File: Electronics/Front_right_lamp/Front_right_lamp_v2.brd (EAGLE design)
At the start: 42.9 x 26.7 mm, 9 parts

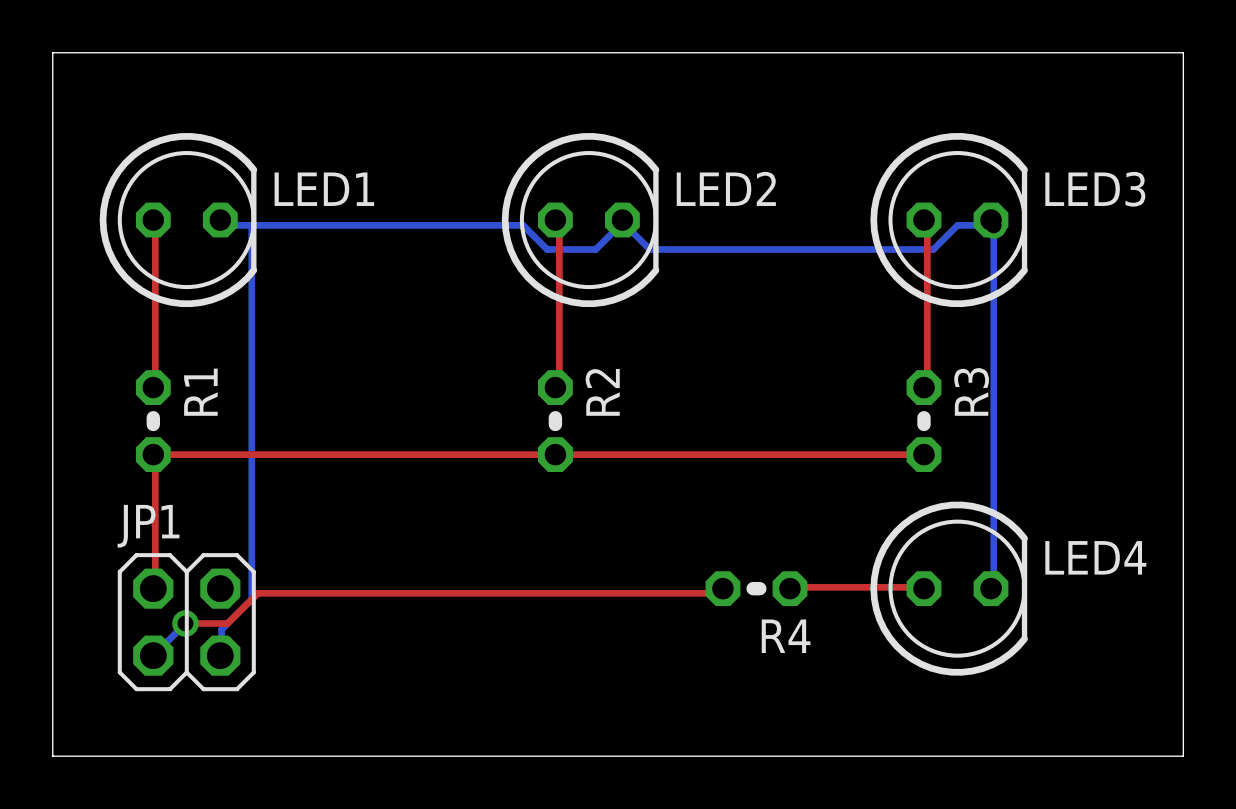
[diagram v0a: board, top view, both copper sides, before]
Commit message: Front lamps done
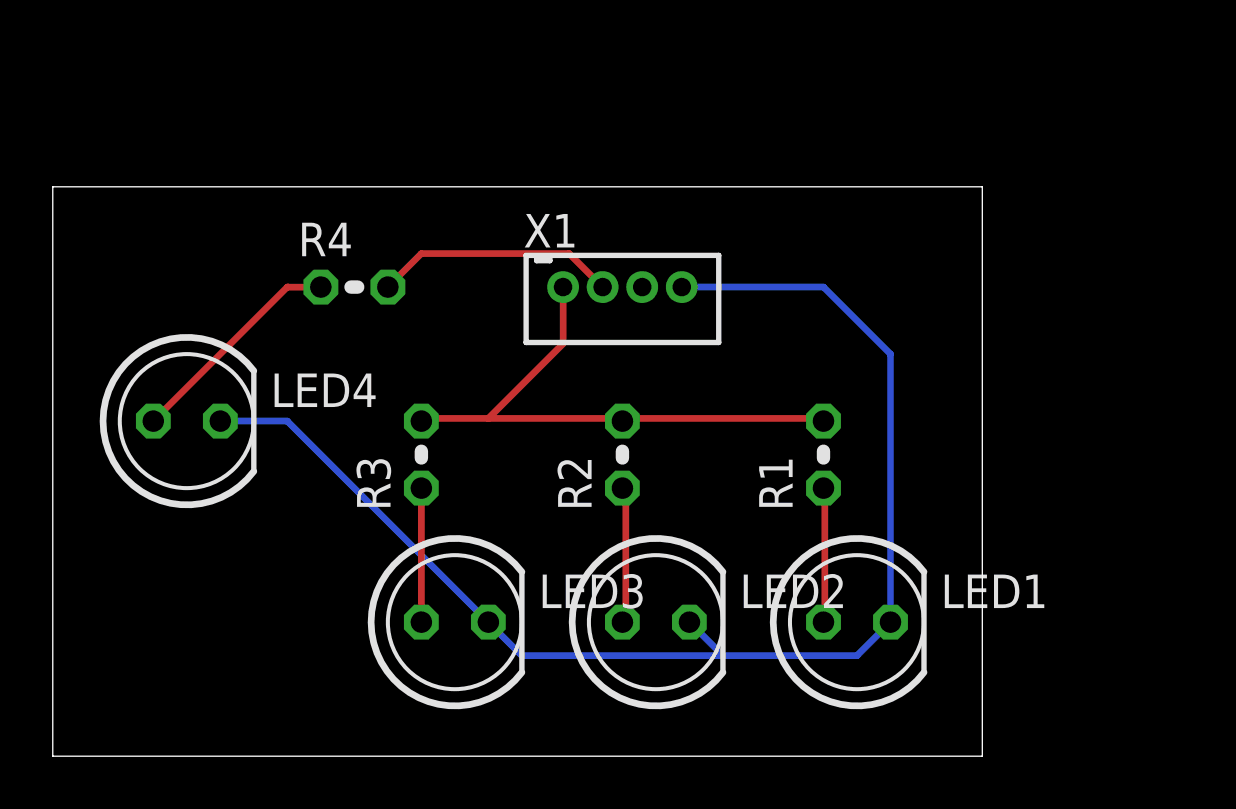
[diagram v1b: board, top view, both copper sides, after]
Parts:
- removed JP1: 2X2, pinhead:2X02
- added X1: B4B-ZR, con-jst:B4B-ZR
- LED1, LED2, LED3: value 2.58V -> 2.58 V
- LED4: value 2.88V -> 1.88 V
- R4: value 1K -> 680
- moved LED4 29.9 mm to (5.08, 12.7)
- moved LED1 29.6 mm to (30.5, 5.08)
- moved R1 25.4 mm to (29.2, 11.4), turned to 90 degrees
- moved LED3 24.4 mm to (15.2, 5.08)
- moved R3 19.1 mm to (14.0, 11.4), turned to 90 degrees
- moved R4 19.1 mm to (11.4, 17.8), turned to 0 degrees
- moved LED2 15.5 mm to (22.9, 5.08)
- moved R2 2.84 mm to (21.6, 11.4), turned to 90 degrees
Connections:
- net N$5: now also X1.1; no longer JP1.2
- net N$6: now also X1.2; no longer JP1.1
- net N$7: now also X1.4; no longer JP1.3
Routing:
- net N$6: track 22.7 -> 9.19 mm, vias 1 -> 0
- net N$5: track 34.3 -> 21.5 mm
- net N$7: track 62.1 -> 50.5 mm, vias 2 -> 0
- net N$4: track 5.10 -> 8.45 mm
- net N$3: track 6.42 -> 5.08 mm
- net N$1: track 6.38 -> 5.10 mm
- net N$2: track 6.45 -> 5.18 mm
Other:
- board size 42.9 x 26.7 mm -> 35.2 x 21.6 mm

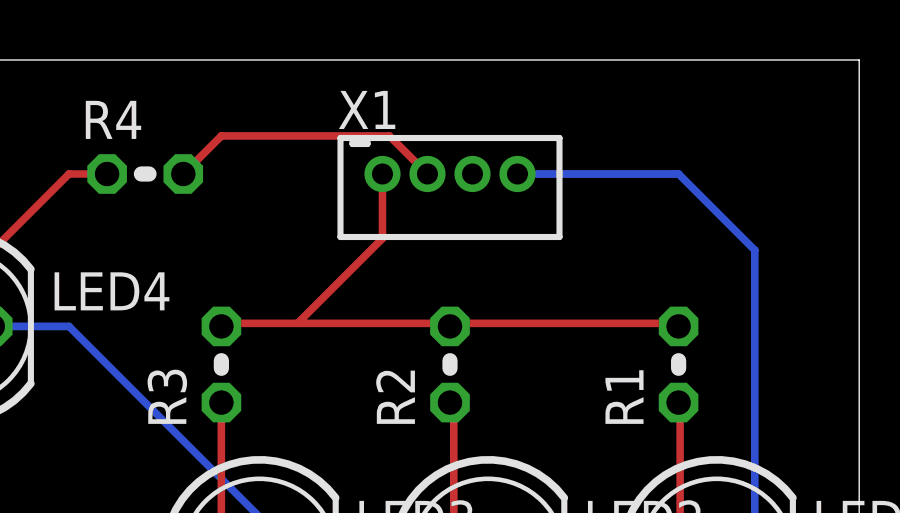
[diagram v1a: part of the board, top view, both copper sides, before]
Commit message: Front and rear lamps done
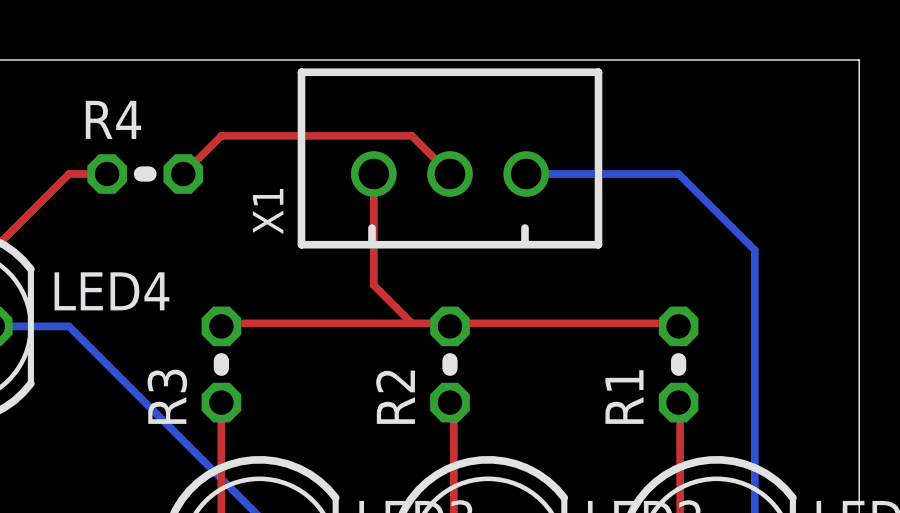
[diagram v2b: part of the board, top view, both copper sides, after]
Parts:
- X1: value B4B-ZR -> JST-XH-03-PIN-ROUND-PAD; device con-jst:B4B-ZR -> Rembrandt Electronics - JST XH Connectors v1-0:JST-XH-03-PACKAGE-ROUND-PAD
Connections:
- net N$5 renamed API_START_ENGINE
- net N$6 renamed API_TURN_RIGHT
- removed net N$7: LED1.K, LED2.K, LED3.K, LED4.K, X1.4
- new net GND: LED1.K, LED2.K, LED3.K, LED4.K, X1.3
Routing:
- net N$7: track 50.5 -> 0.00 mm
- net GND: track 0.00 -> 50.2 mm
- net API_TURN_RIGHT: track 9.19 -> 9.94 mm
- net API_START_ENGINE: track 21.5 -> 20.9 mm
